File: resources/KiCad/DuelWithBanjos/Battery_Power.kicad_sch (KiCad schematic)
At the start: 6 parts, among them J1 Conn_01x03_Pin, J2 Conn_01x03_Socket, SW1 SW_SPST

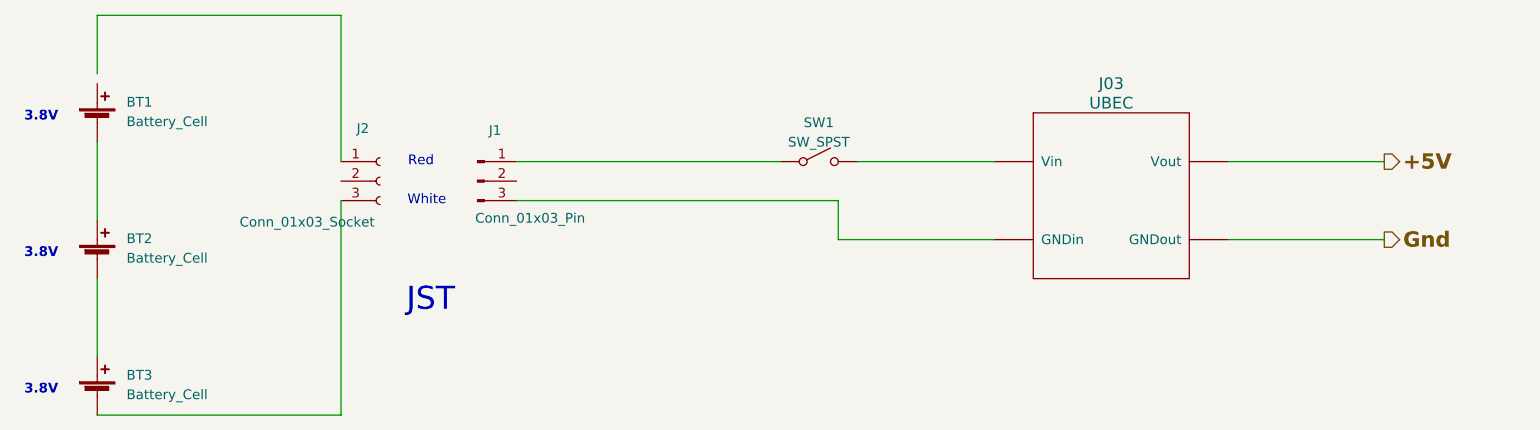
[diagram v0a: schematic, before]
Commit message: V1.0 schematic power update
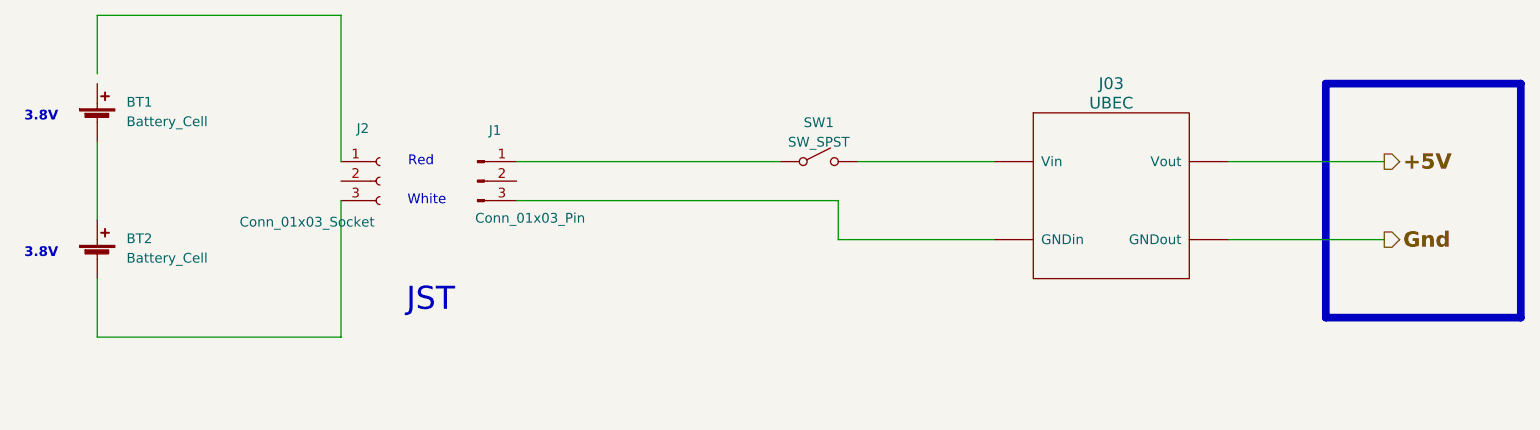
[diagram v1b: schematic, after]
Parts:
- removed BT3: Battery_Cell, symbol Device:Battery_Cell
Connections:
- net at SW1.~ (B): now also J1.1 (Pin_1)
- net at J2.3 (Pin_3): now also BT2.2 (-)
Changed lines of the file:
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@@
 	(title_block
 		(title "DuelWithBanjos")
-		(date "2025-05-08")
-		(rev "Rev 0.9")
+		(date "2025-06-08")
+		(rev "Rev 1.0")
 		(company "https://github.com/Mark-MDO47")
 	)
+	(rectangle
+		(start 198.12 58.42)
+		(end 223.52 88.9)
+		(stroke
+			(width 1)
+			(type solid)
+		)
+		(fill
+			(type none)
+		)
+	)
 	(text "Red"
 		(exclude_from_sim no)
@@
 	(text "3.8V"
 		(exclude_from_sim no)
-		(at 33.02 99.06 0)
+		(at 33.02 81.28 0)
 		(effects
 			(font
@@
 	(text "3.8V"
 		(exclude_from_sim no)
-		(at 33.02 81.28 0)
+		(at 33.02 63.5 0)
 		(effects
 			(font
@@
 		)
 	)
-	(text "3.8V"
-		(exclude_from_sim no)
-		(at 33.02 63.5 0)
-		(effects
-			(font
-				(size 1.27 1.27)
-				(bold yes)
-			)
-			(justify right bottom)
-		)
-	)
-	(wire
-		(pts
-			(xy 69.85 101.6) (xy 69.85 73.66)
-		)
-		(stroke
-			(width 0)
-			(type default)
-		)
-	)
 	(wire
 		(pts
@@
 	(wire
 		(pts
-			(xy 38.1 83.82) (xy 38.1 93.98)
-		)
-		(stroke
-			(width 0)
-			(type default)
-		)
-	)
-	(wire
-		(pts
 			(xy 38.1 66.04) (xy 38.1 76.2)
 		)
@@
 	(wire
 		(pts
-			(xy 38.1 101.6) (xy 69.85 101.6)
-		)
-		(stroke
-			(width 0)
-			(type default)
-		)
-	)
-	(wire
-		(pts
 			(xy 92.71 73.66) (xy 134.62 73.66)
 		)
@@
 	(wire
 		(pts
+			(xy 38.1 83.82) (xy 38.1 91.44)
+		)
+		(stroke
+			(width 0)
+			(type default)
+		)
+	)
+	(wire
+		(pts
 			(xy 137.16 68.58) (xy 154.94 68.58)
 		)
@@
 		(pts
 			(xy 69.85 49.53) (xy 69.85 68.58)
+		)
+		(stroke
+			(width 0)
+			(type default)
+		)
+	)
+	(wire
+		(pts
+			(xy 38.1 91.44) (xy 69.85 91.44)
+		)
+		(stroke
+			(width 0)
+			(type default)
+		)
+	)
+	(wire
+		(pts
+			(xy 69.85 91.44) (xy 69.85 73.66)
 		)
 		(stroke
@@
 					(unit 1)
 				)
-			)
-		)
-	)
-	(symbol
-		(lib_id "Device:Battery_Cell")
-		(at 38.1 99.06 0)
-		(unit 1)
-		(exclude_from_sim no)
-		(in_bom yes)
-		(on_board yes)
-		(dnp no)
-		(fields_autoplaced yes)
-		(property "Reference" "BT3"
-			(at 41.91 96.393 0)
-			(effects
-				(font
-					(size 1.27 1.27)
-				)
-				(justify left)
-			)
-		)
-		(property "Value" "Battery_Cell"
-			(at 41.91 98.933 0)
-			(effects
-				(font
-					(size 1.27 1.27)
-				)
-				(justify left)
-			)
-		)
-		(property "Footprint" ""
-			(at 38.1 97.536 90)
-			(effects
-				(font
-					(size 1.27 1.27)
-				)
-				(hide yes)
-			)
-		)
-		(property "Datasheet" "~"
-			(at 38.1 97.536 90)
-			(effects
-				(font
-					(size 1.27 1.27)
-				)
-				(hide yes)
-			)
-		)
-		(property "Description" ""
-			(at 38.1 99.06 0)
-			(effects
-				(font
-					(size 1.27 1.27)
-				)
-				(hide yes)
-			)
-		)
-		(pin "1"
-		)
-		(pin "2"
-		)
-		(instances
-			(project "DuelWithBanjos"
-				(path "/c9b0a009-eaf9-4c5a-9c22-a228fddea57d/bc1c1418-3098-4af1-89ea-7f31e7186f1b"
-					(reference "BT3")
-					(unit 1)
-				)
